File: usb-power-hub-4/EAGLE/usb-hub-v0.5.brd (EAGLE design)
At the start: 95 x 25 mm, 37 parts, among them U1 RICHTEKRT9715AGBR, U2 RICHTEKRT9715AGBR, U3 RICHTEKRT9715AGBR, U4 RICHTEKRT9715AGBR

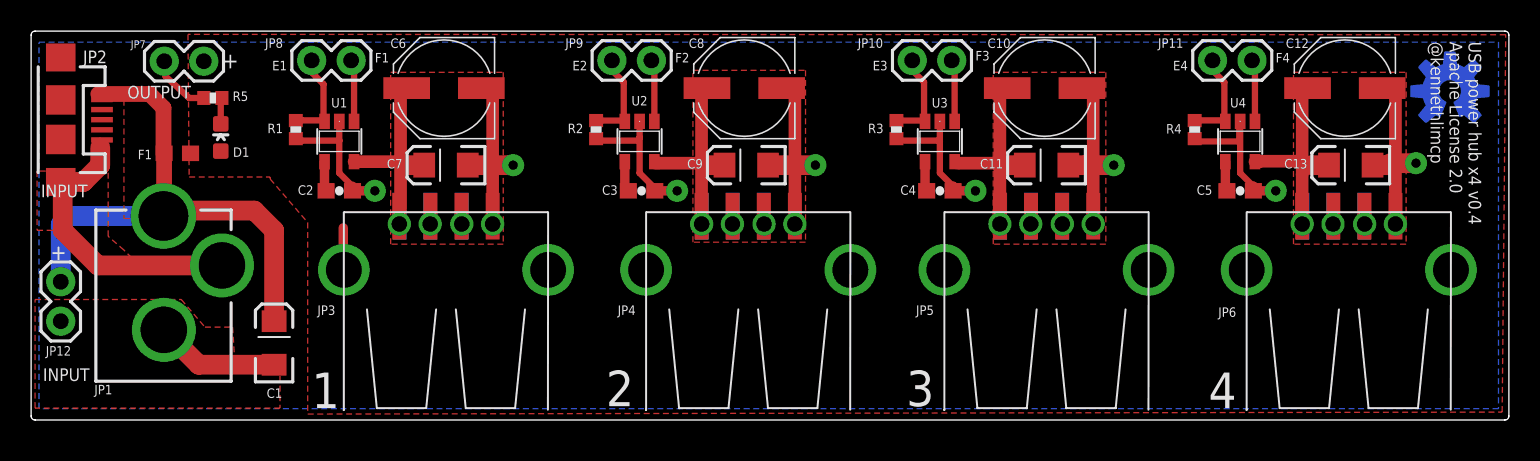
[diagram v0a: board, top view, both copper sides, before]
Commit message: V0.5 update!
Fixed an important issue of USB A through hole spacing being too
narrow.

This should be a golden version since first fabrication!
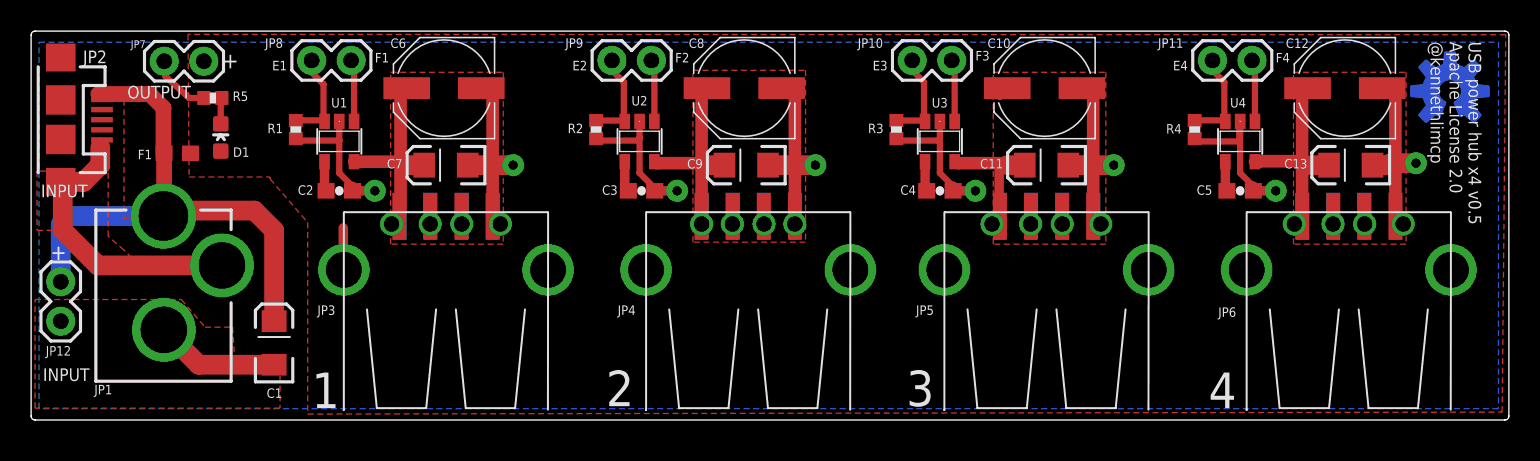
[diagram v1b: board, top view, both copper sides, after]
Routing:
- net VOUT3: track 17.5 -> 9.76 mm
- net GND: vias 12 -> 10
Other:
- board text added: "USB power hub x4 v0.5 Apache License 2.0 @kennethlimcp"
- board text removed: "USB power hub x4 v0.4 Apache License 2.0 @kennethlimcp"
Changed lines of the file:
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@@
 <setting verticaltext="up"/>
 </settings>
-<grid distance="5" unitdist="mil" unit="mil" style="lines" multiple="1" display="yes" altdistance="1" altunitdist="mm" altunit="mm"/>
+<grid distance="1" unitdist="mm" unit="mm" style="lines" multiple="1" display="yes" altdistance="1" altunitdist="mm" altunit="mm"/>
 <layers>
-<layer number="1" name="Top" color="4" fill="1" visible="yes" active="yes"/>
+<layer number="1" name="Top" color="4" fill="1" visible="no" active="yes"/>
 <layer number="2" name="Route2" color="1" fill="3" visible="no" active="yes"/>
 <layer number="3" name="Route3" color="4" fill="3" visible="no" active="no"/>
@@
 <rectangle x1="46.6598" y1="11.6078" x2="47.5488" y2="14.605" layer="16"/>
 <rectangle x1="44.6532" y1="11.6078" x2="45.5422" y2="14.605" layer="16"/>
-<rectangle x1="42.672" y1="11.6078" x2="43.561" y2="14.605" layer="16"/>
 <rectangle x1="65.8368" y1="11.6078" x2="66.7258" y2="14.605" layer="16"/>
 <rectangle x1="63.8302" y1="11.6078" x2="64.7192" y2="14.605" layer="16"/>
@@
 <text x="56.261" y="0.889" size="2.286" layer="25" font="vector" ratio="15">3</text>
 <text x="75.692" y="0.762" size="2.286" layer="25" font="vector" ratio="15">4</text>
-<text x="89.967" y="24.323" size="0.8128" layer="25" font="vector" ratio="20" rot="SR270">USB power hub x4 v0.4
+<text x="89.967" y="24.323" size="0.8128" layer="25" font="vector" ratio="20" rot="SR270">USB power hub x4 v0.5
 Apache License 2.0
 @kennethlimcp
@@
 <rectangle x1="67.7164" y1="11.4554" x2="68.8594" y2="14.7574" layer="30"/>
 <rectangle x1="87.1474" y1="11.4554" x2="88.2904" y2="14.7574" layer="30"/>
+<rectangle x1="42.6532" y1="11.6078" x2="43.5422" y2="14.605" layer="16"/>
+<rectangle x1="48.6598" y1="11.6078" x2="49.5488" y2="14.605" layer="16"/>
+<rectangle x1="29.2288" y1="11.6078" x2="30.1178" y2="14.605" layer="16"/>
+<rectangle x1="67.8368" y1="11.6078" x2="68.7258" y2="14.605" layer="16"/>
+<rectangle x1="87.2678" y1="11.6078" x2="88.1568" y2="14.605" layer="16"/>
 </plain>
 <attributes>
@@
 <wire x1="87.709" y1="21.257" x2="87.7062" y2="21.257" width="0.6096" layer="1"/>
 <wire x1="87.7062" y1="21.257" x2="87.7062" y2="16.256" width="0.8128" layer="1"/>
-<via x="29.6672" y="12.5984" extent="1-16" drill="1" diameter="0.6"/>
+<via x="30.1672" y="12.5984" extent="1-16" drill="1" diameter="0.6"/>
 <contactref element="JP7" pad="2"/>
 <wire x1="87.7062" y1="16.256" x2="87.7062" y2="14.1224" width="0.8128" layer="1"/>
@@
 <wire x1="49.022" y1="21.336" x2="48.247" y2="21.336" width="0.4064" layer="1"/>
 <via x="49.0982" y="12.5984" extent="1-16" drill="1" diameter="0.6"/>
-<via x="68.2752" y="12.5984" extent="1-16" drill="1" diameter="0.6"/>
-<via x="87.7062" y="12.5984" extent="1-16" drill="1" diameter="0.6"/>
 <wire x1="19.812" y1="17.962" x2="17.399" y2="17.962" width="0.4064" layer="1"/>
 <wire x1="17.399" y1="17.962" x2="17.018" y2="18.089" width="0.4064" layer="1"/>
@@
 <wire x1="77.597" y1="17.907" x2="74.985" y2="17.907" width="0.4064" layer="1"/>
 <wire x1="74.985" y1="17.907" x2="74.803" y2="18.089" width="0.4064" layer="1"/>
+<wire x1="49.101" y1="13.102" x2="49.0982" y2="12.5984" width="0" layer="19" extent="1-1"/>
 </signal>
 <signal name="GND-ISO">
@@
 <contactref element="C10" pad="+"/>
 <contactref element="C11" pad="A"/>
-<wire x1="62.278" y1="13.102" x2="62.278" y2="20.863" width="0.8128" layer="1"/>
 <wire x1="62.278" y1="20.863" x2="62.751" y2="21.336" width="0.6096" layer="1"/>
 <wire x1="63.878" y1="16.383" x2="62.738" y2="16.383" width="1.27" layer="1"/>
@@
 <wire x1="62.278" y1="13.102" x2="62.23" y2="13.277" width="0.6096" layer="1"/>
 <wire x1="62.23" y1="13.277" x2="62.23" y2="16.51" width="0.6096" layer="1"/>
+<wire x1="62.23" y1="16.51" x2="62.278" y2="20.863" width="0" layer="19" extent="1-1"/>
 </signal>
 <signal name="VOUT4">
@@
 </signal>
 <signal name="N$6">
-<via x="23.6728" y="12.5984" extent="1-16" drill="1" diameter="0.6"/>
+<via x="23.1728" y="12.5984" extent="1-16" drill="1" diameter="0.6"/>
 <via x="25.654" y="12.5984" extent="1-16" drill="1" diameter="0.6"/>
 <via x="27.686" y="12.5984" extent="1-16" drill="1" diameter="0.6"/>
-<wire x1="23.6728" y1="12.5984" x2="25.654" y2="12.5984" width="0" layer="19" extent="1-1"/>
 <wire x1="27.686" y1="12.5984" x2="25.654" y2="12.5984" width="0" layer="19" extent="1-1"/>
+<wire x1="23.1728" y1="12.5984" x2="25.654" y2="12.5984" width="0" layer="19" extent="1-1"/>
 </signal>
 <signal name="N$8">
@@
 </signal>
 <signal name="N$2">
-<via x="81.7118" y="12.5984" extent="1-16" drill="1" diameter="0.6"/>
 <via x="83.693" y="12.5984" extent="1-16" drill="1" diameter="0.6"/>
 <via x="85.725" y="12.5984" extent="1-16" drill="1" diameter="0.6"/>
 <wire x1="83.693" y1="12.5984" x2="85.725" y2="12.5984" width="0" layer="19" extent="1-1"/>
-<wire x1="81.7118" y1="12.5984" x2="83.693" y2="12.5984" width="0" layer="19" extent="1-1"/>
 </signal>
 <signal name="N$3">
 <via x="43.1038" y="12.5984" extent="1-16" drill="1" diameter="0.6"/>
-<via x="45.085" y="12.5984" extent="1-16" drill="1" diameter="0.6"/>
-<via x="47.117" y="12.5984" extent="1-16" drill="1" diameter="0.6"/>
-<wire x1="45.085" y1="12.5984" x2="47.117" y2="12.5984" width="0" layer="19" extent="1-1"/>
-<wire x1="43.1038" y1="12.5984" x2="45.085" y2="12.5984" width="0" layer="19" extent="1-1"/>
-</signal>
-<signal name="N$4">
-<via x="62.2808" y="12.5984" extent="1-16" drill="1" diameter="0.6"/>
-<via x="64.262" y="12.5984" extent="1-16" drill="1" diameter="0.6"/>
-<via x="66.294" y="12.5984" extent="1-16" drill="1" diameter="0.6"/>
-<wire x1="64.262" y1="12.5984" x2="66.294" y2="12.5984" width="0" layer="19" extent="1-1"/>
-<wire x1="62.2808" y1="12.5984" x2="64.262" y2="12.5984" width="0" layer="19" extent="1-1"/>
 </signal>
 <signal name="N$5">
@@
 <wire x1="12.192" y1="20.502" x2="12.264" y2="20.701" width="0.4064" layer="1"/>
 </signal>
+<signal name="GND4">
+<via x="88.2072" y="12.5984" extent="1-16" drill="1" diameter="0.6"/>
+</signal>
+<signal name="VOUT5">
+</signal>
+<signal name="N$7">
+<via x="81.2128" y="12.5984" extent="1-16" drill="1" diameter="0.6"/>
+</signal>
+<signal name="N$9">
+<via x="45.084" y="12.5984" extent="1-16" drill="1" diameter="0.6"/>
+<via x="47.116" y="12.5984" extent="1-16" drill="1" diameter="0.6"/>
+<wire x1="45.084" y1="12.5984" x2="47.116" y2="12.5984" width="0" layer="19" extent="1-1"/>
+</signal>
+<signal name="GND5">
+<via x="68.7672" y="12.5984" extent="1-16" drill="1" diameter="0.6"/>
+</signal>
+<signal name="N$11">
+<via x="61.7728" y="12.5984" extent="1-16" drill="1" diameter="0.6"/>
+<via x="64.254" y="12.5984" extent="1-16" drill="1" diameter="0.6"/>
+<via x="66.286" y="12.5984" extent="1-16" drill="1" diameter="0.6"/>
+<wire x1="64.254" y1="12.5984" x2="66.286" y2="12.5984" width="0" layer="19" extent="1-1"/>
+<wire x1="61.7728" y1="12.5984" x2="64.254" y2="12.5984" width="0" layer="19" extent="1-1"/>
+</signal>
 </signals>

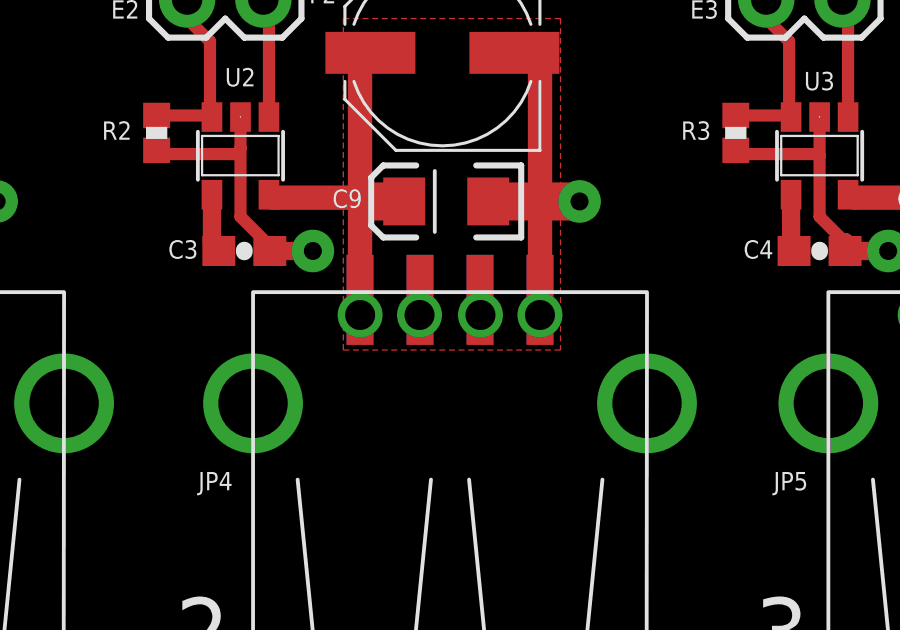
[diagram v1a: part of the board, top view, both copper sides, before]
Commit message: fixed wrong via net and missing port 2 correction
ghhhhh….
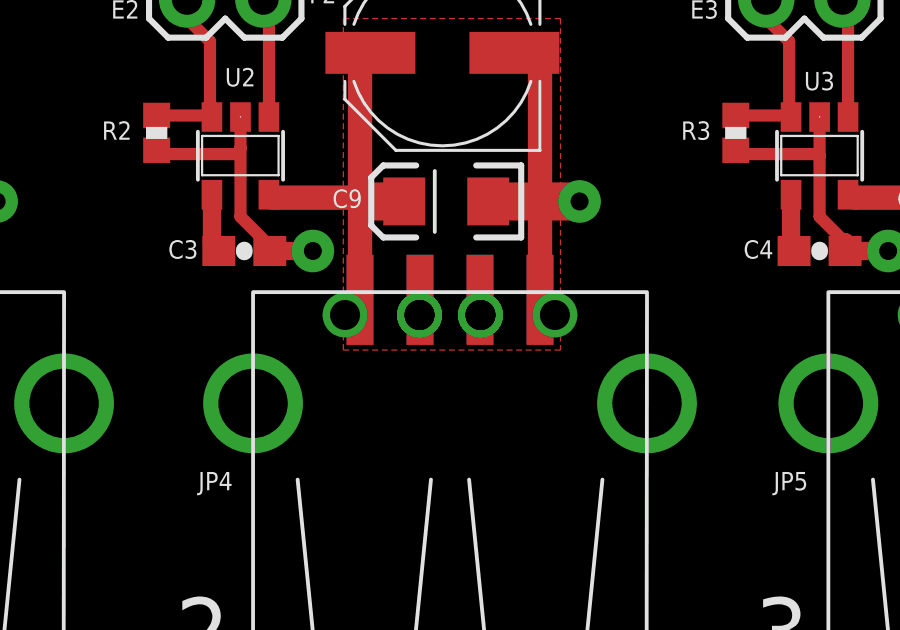
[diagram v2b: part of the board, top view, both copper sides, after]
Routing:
- net GND: vias 10 -> 12
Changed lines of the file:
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@@
 <setting verticaltext="up"/>
 </settings>
-<grid distance="1" unitdist="mm" unit="mm" style="lines" multiple="1" display="yes" altdistance="1" altunitdist="mm" altunit="mm"/>
+<grid distance="0.01" unitdist="mm" unit="mm" style="lines" multiple="1" display="yes" altdistance="1" altunitdist="mm" altunit="mm"/>
 <layers>
 <layer number="1" name="Top" color="4" fill="1" visible="no" active="yes"/>
@@
 <layer number="17" name="Pads" color="2" fill="1" visible="yes" active="yes"/>
 <layer number="18" name="Vias" color="2" fill="1" visible="yes" active="yes"/>
-<layer number="19" name="Unrouted" color="6" fill="1" visible="yes" active="yes"/>
-<layer number="20" name="Dimension" color="15" fill="1" visible="yes" active="yes"/>
-<layer number="21" name="tPlace" color="7" fill="1" visible="yes" active="yes"/>
+<layer number="19" name="Unrouted" color="6" fill="1" visible="no" active="yes"/>
+<layer number="20" name="Dimension" color="15" fill="1" visible="no" active="yes"/>
+<layer number="21" name="tPlace" color="7" fill="1" visible="no" active="yes"/>
 <layer number="22" name="bPlace" color="7" fill="1" visible="no" active="yes"/>
-<layer number="23" name="tOrigins" color="15" fill="1" visible="no" active="yes"/>
-<layer number="24" name="bOrigins" color="15" fill="1" visible="yes" active="yes"/>
-<layer number="25" name="tNames" color="7" fill="1" visible="yes" active="yes"/>
+<layer number="23" name="tOrigins" color="15" fill="1" visible="yes" active="yes"/>
+<layer number="24" name="bOrigins" color="15" fill="1" visible="no" active="yes"/>
+<layer number="25" name="tNames" color="7" fill="1" visible="no" active="yes"/>
 <layer number="26" name="bNames" color="7" fill="1" visible="no" active="yes"/>
 <layer number="27" name="tValues" color="7" fill="1" visible="no" active="yes"/>
 <layer number="28" name="bValues" color="7" fill="1" visible="no" active="yes"/>
 <layer number="29" name="tStop" color="7" fill="3" visible="no" active="yes"/>
-<layer number="30" name="bStop" color="7" fill="6" visible="yes" active="yes"/>
+<layer number="30" name="bStop" color="7" fill="6" visible="no" active="yes"/>
 <layer number="31" name="tCream" color="7" fill="4" visible="no" active="yes"/>
 <layer number="32" name="bCream" color="7" fill="5" visible="no" active="yes"/>
@@
 <wire x1="87.63" y1="21.336" x2="86.855" y2="21.336" width="0.4064" layer="1"/>
 <wire x1="49.022" y1="21.336" x2="48.247" y2="21.336" width="0.4064" layer="1"/>
-<via x="49.0982" y="12.5984" extent="1-16" drill="1" diameter="0.6"/>
 <wire x1="19.812" y1="17.962" x2="17.399" y2="17.962" width="0.4064" layer="1"/>
 <wire x1="17.399" y1="17.962" x2="17.018" y2="18.089" width="0.4064" layer="1"/>
@@
 <wire x1="77.597" y1="17.907" x2="74.985" y2="17.907" width="0.4064" layer="1"/>
 <wire x1="74.985" y1="17.907" x2="74.803" y2="18.089" width="0.4064" layer="1"/>
-<wire x1="49.101" y1="13.102" x2="49.0982" y2="12.5984" width="0" layer="19" extent="1-1"/>
+<via x="88.2072" y="12.5984" extent="1-16" drill="1" diameter="0.6"/>
+<via x="68.7672" y="12.5984" extent="1-16" drill="1" diameter="0.6"/>
+<via x="49.5972" y="12.5984" extent="1-16" drill="1" diameter="0.6"/>
+<wire x1="49.101" y1="13.102" x2="49.5972" y2="12.5984" width="0" layer="19" extent="1-1"/>
 </signal>
 <signal name="GND-ISO">
@@
 <wire x1="83.693" y1="12.5984" x2="85.725" y2="12.5984" width="0" layer="19" extent="1-1"/>
 </signal>
-<signal name="N$3">
-<via x="43.1038" y="12.5984" extent="1-16" drill="1" diameter="0.6"/>
-</signal>
 <signal name="N$5">
 <contactref element="D1" pad="C"/>
@@
 <wire x1="12.192" y1="20.502" x2="12.264" y2="20.701" width="0.4064" layer="1"/>
 </signal>
-<signal name="GND4">
-<via x="88.2072" y="12.5984" extent="1-16" drill="1" diameter="0.6"/>
-</signal>
 <signal name="VOUT5">
 </signal>
@@
 <via x="47.116" y="12.5984" extent="1-16" drill="1" diameter="0.6"/>
 <wire x1="45.084" y1="12.5984" x2="47.116" y2="12.5984" width="0" layer="19" extent="1-1"/>
-</signal>
-<signal name="GND5">
-<via x="68.7672" y="12.5984" extent="1-16" drill="1" diameter="0.6"/>
 </signal>
 <signal name="N$11">
@@
 <wire x1="61.7728" y1="12.5984" x2="64.254" y2="12.5984" width="0" layer="19" extent="1-1"/>
 </signal>
+<signal name="N$4">
+<via x="42.6028" y="12.5984" extent="1-16" drill="1" diameter="0.6"/>
+<via x="45.084" y="12.5984" extent="1-16" drill="1" diameter="0.6"/>
+<via x="47.116" y="12.5984" extent="1-16" drill="1" diameter="0.6"/>
+<wire x1="45.084" y1="12.5984" x2="47.116" y2="12.5984" width="0" layer="19" extent="1-1"/>
+<wire x1="42.6028" y1="12.5984" x2="45.084" y2="12.5984" width="0" layer="19" extent="1-1"/>
+</signal>
 </signals>
